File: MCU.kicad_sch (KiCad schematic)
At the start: 30 parts, among them J1 HSEC8-150-01-X-RA-X, J17 Conn_02x30_Counter_Clockwise, J2 Barrel_Jack_MountingPin, J22 Conn_01x02, J23 Conn_01x02, J4 Conn_02x30_Counter_Clockwise, J6 Conn_01x02, U3 LMR36510ADDA

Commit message: Validated for prod
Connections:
- net PE10_EXTI10: no longer names the net of J4.39 (Pin_39)
- no-connect marks 17 -> 24
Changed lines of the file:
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@@
 	)
 	(no_connect
+		(at 190.5 262.89)
+	)
+	(no_connect
+		(at 190.5 265.43)
+	)
+	(no_connect
 		(at 167.64 78.74)
 	)
@@
 	)
 	(no_connect
+		(at 95.25 245.11)
+	)
+	(no_connect
 		(at 116.84 63.5)
 	)
 	(no_connect
+		(at 95.25 247.65)
+	)
+	(no_connect
 		(at 116.84 81.28)
 	)
@@
 	)
 	(no_connect
+		(at 95.25 252.73)
+	)
+	(no_connect
 		(at 91.44 45.72)
 	)
@@
 	)
 	(no_connect
+		(at 95.25 255.27)
+	)
+	(no_connect
 		(at 193.04 68.58)
 	)
@@
 		(at 91.44 91.44)
 	)
+	(no_connect
+		(at 190.5 260.35)
+	)
 	(wire
 		(pts
@@
 	(wire
 		(pts
-			(xy 118.11 99.06) (xy 116.84 99.06)
+			(xy 116.84 99.06) (xy 119.38 99.06)
 		)
 		(stroke
@@
 	(wire
 		(pts
-			(xy 116.84 96.52) (xy 118.11 96.52)
+			(xy 116.84 96.52) (xy 119.38 96.52)
 		)
 		(stroke
@@
 	(wire
 		(pts
-			(xy 116.84 55.88) (xy 118.11 55.88)
+			(xy 116.84 55.88) (xy 119.38 55.88)
 		)
 		(stroke
@@
 	(wire
 		(pts
-			(xy 116.84 68.58) (xy 118.11 68.58)
+			(xy 116.84 68.58) (xy 119.38 68.58)
 		)
 		(stroke
@@
 	(wire
 		(pts
-			(xy 116.84 91.44) (xy 118.11 91.44)
+			(xy 116.84 91.44) (xy 119.38 91.44)
 		)
 		(stroke
@@
 	(wire
 		(pts
-			(xy 95.25 245.11) (xy 99.06 245.11)
-		)
-		(stroke
-			(width 0)
-			(type default)
-		)
-	)
-	(wire
-		(pts
 			(xy 187.96 229.87) (xy 190.5 229.87)
 		)
@@
 	(wire
 		(pts
-			(xy 116.84 53.34) (xy 118.11 53.34)
+			(xy 116.84 53.34) (xy 119.38 53.34)
 		)
 		(stroke
@@
 	(wire
 		(pts
-			(xy 116.84 88.9) (xy 118.11 88.9)
+			(xy 116.84 88.9) (xy 119.38 88.9)
 		)
 		(stroke
@@
 	(wire
 		(pts
-			(xy 116.84 71.12) (xy 118.11 71.12)
+			(xy 116.84 71.12) (xy 119.38 71.12)
 		)
 		(stroke
@@
 	(wire
 		(pts
-			(xy 116.84 78.74) (xy 118.11 78.74)
+			(xy 116.84 78.74) (xy 119.38 78.74)
 		)
 		(stroke
@@
 	(global_label "ISOSW_HOLD_CMD"
 		(shape input)
-		(at 118.11 99.06 0)
+		(at 119.38 99.06 0)
 		(fields_autoplaced yes)
 		(effects
@@
 		)
 		(property "Intersheetrefs" "${INTERSHEET_REFS}"
-			(at 141.1732 99.06 0)
+			(at 142.4432 99.06 0)
 			(hide yes)
 			(show_name no)
@@
 	(global_label "ISOSW_OF_ST"
 		(shape input)
-		(at 118.11 88.9 0)
+		(at 119.38 88.9 0)
 		(fields_autoplaced yes)
 		(effects
@@
 		)
 		(property "Intersheetrefs" "${INTERSHEET_REFS}"
-			(at 136.8189 88.9 0)
+			(at 138.0889 88.9 0)
 			(hide yes)
 			(show_name no)
@@
 	(global_label "A0V"
 		(shape input)
-		(at 118.11 71.12 0)
+		(at 119.38 71.12 0)
 		(fields_autoplaced yes)
 		(effects
@@
 		)
 		(property "Intersheetrefs" "${INTERSHEET_REFS}"
-			(at 124.4819 71.12 0)
+			(at 125.7519 71.12 0)
 			(hide yes)
 			(show_name no)
@@
 	(global_label "PADLOCK_OF"
 		(shape input)
-		(at 118.11 96.52 0)
+		(at 119.38 96.52 0)
 		(fields_autoplaced yes)
 		(effects
@@
 		)
 		(property "Intersheetrefs" "${INTERSHEET_REFS}"
-			(at 136.3957 96.52 0)
+			(at 137.6657 96.52 0)
 			(hide yes)
 			(show_name no)
@@
 		)
 	)
-	(global_label "PE10_EXTI10"
-		(shape input)
-		(at 99.06 245.11 0)
-		(fields_autoplaced yes)
-		(effects
-			(font
-				(size 1.27 1.27)
-			)
-			(justify left)
-		)
-		(property "Intersheetrefs" "${INTERSHEET_REFS}"
-			(at 114.2007 245.11 0)
-			(hide yes)
-			(show_name no)
-			(do_not_autoplace no)
-			(effects
-				(font
-					(size 1.27 1.27)
-				)
-				(justify left)
-			)
-		)
-	)
 	(global_label "V_ACT"
 		(shape input)
@@
 	(global_label "SDMOS"
 		(shape input)
-		(at 118.11 68.58 0)
+		(at 119.38 68.58 0)
 		(fields_autoplaced yes)
 		(effects
@@
 		)
 		(property "Intersheetrefs" "${INTERSHEET_REFS}"
-			(at 130.9527 68.58 0)
+			(at 132.2227 68.58 0)
 			(hide yes)
 			(show_name no)
@@
 	(global_label "VPS_P24V_PG"
 		(shape input)
-		(at 118.11 78.74 0)
+		(at 119.38 78.74 0)
 		(fields_autoplaced yes)
 		(effects
@@
 		)
 		(property "Intersheetrefs" "${INTERSHEET_REFS}"
-			(at 137.3027 78.74 0)
+			(at 138.5727 78.74 0)
 			(hide yes)
 			(show_name no)
@@
 	(global_label "OPCL_DS"
 		(shape input)
-		(at 118.11 53.34 0)
+		(at 119.38 53.34 0)
 		(fields_autoplaced yes)
 		(effects
@@
 		)
 		(property "Intersheetrefs" "${INTERSHEET_REFS}"
-			(at 132.8275 53.34 0)
+			(at 134.0975 53.34 0)
 			(hide yes)
 			(show_name no)
@@
 	(global_label "A0V"
 		(shape input)
-		(at 118.11 55.88 0)
+		(at 119.38 55.88 0)
 		(fields_autoplaced yes)
 		(effects
@@
 		)
 		(property "Intersheetrefs" "${INTERSHEET_REFS}"
-			(at 124.4819 55.88 0)
+			(at 125.7519 55.88 0)
 			(hide yes)
 			(show_name no)
@@
 	(global_label "ISOSW_INRUSH_CMD"
 		(shape input)
-		(at 118.11 91.44 0)
+		(at 119.38 91.44 0)
 		(fields_autoplaced yes)
 		(effects
@@
 		)
 		(property "Intersheetrefs" "${INTERSHEET_REFS}"
-			(at 143.2899 91.44 0)
+			(at 144.5599 91.44 0)
 			(hide yes)
 			(show_name no)

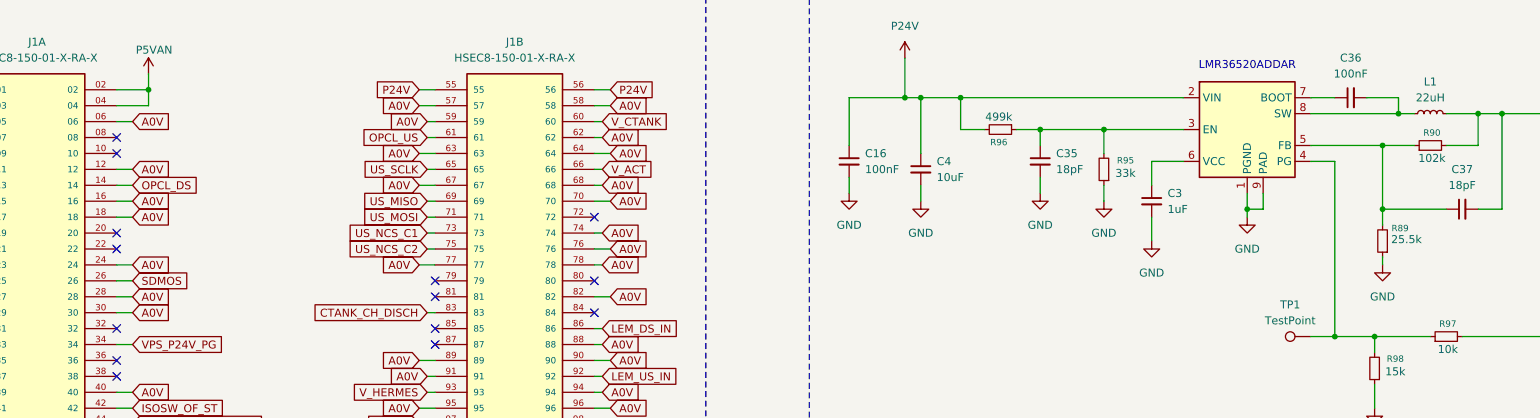
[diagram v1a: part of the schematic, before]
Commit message: breakout typo
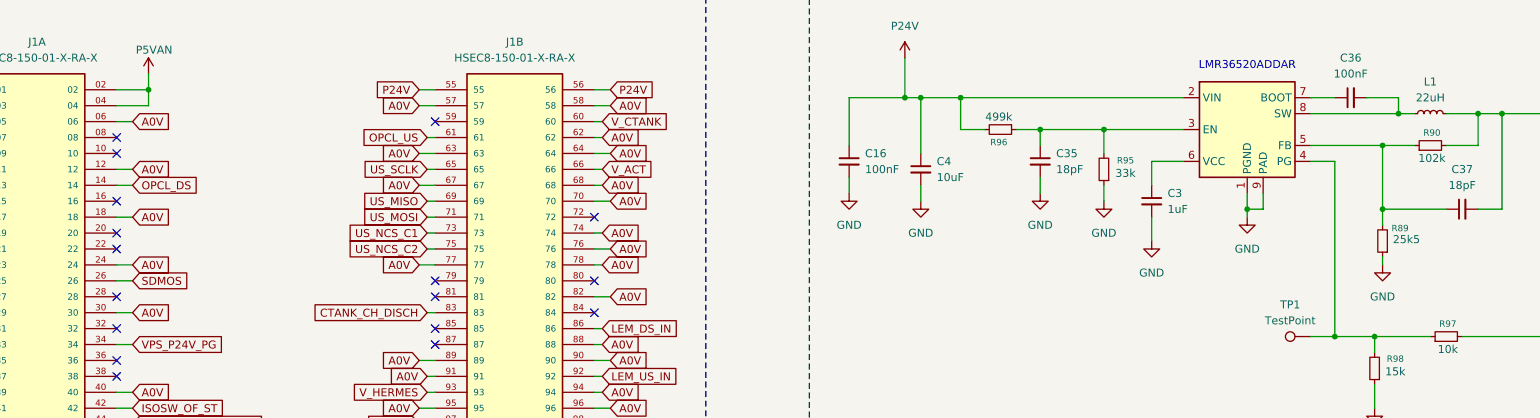
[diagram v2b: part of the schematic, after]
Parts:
- R89: value 25.5k -> 25k5
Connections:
- net GND: no longer J1.16, J1.28, J1.59
- no-connect marks 24 -> 27
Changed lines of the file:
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@@
 	)
 	(no_connect
+		(at 167.64 43.18)
+	)
+	(no_connect
 		(at 193.04 58.42)
 	)
@@
 	)
 	(no_connect
+		(at 116.84 55.88)
+	)
+	(no_connect
 		(at 116.84 60.96)
 	)
@@
 	)
 	(no_connect
+		(at 116.84 71.12)
+	)
+	(no_connect
 		(at 190.5 260.35)
 	)
@@
 	(wire
 		(pts
-			(xy 116.84 55.88) (xy 119.38 55.88)
-		)
-		(stroke
-			(width 0)
-			(type default)
-		)
-	)
-	(wire
-		(pts
 			(xy 167.64 91.44) (xy 165.1 91.44)
 		)
@@
 	(wire
 		(pts
-			(xy 116.84 71.12) (xy 119.38 71.12)
-		)
-		(stroke
-			(width 0)
-			(type default)
-		)
-	)
-	(wire
-		(pts
 			(xy 80.01 222.25) (xy 82.55 222.25)
 		)
@@
 	(wire
 		(pts
-			(xy 167.64 43.18) (xy 166.37 43.18)
-		)
-		(stroke
-			(width 0)
-			(type default)
-		)
-	)
-	(wire
-		(pts
 			(xy 255.27 44.45) (xy 251.46 44.45)
 		)
@@
 		)
 	)
-	(global_label "A0V"
-		(shape input)
-		(at 166.37 43.18 180)
-		(fields_autoplaced yes)
-		(effects
-			(font
-				(size 1.27 1.27)
-			)
-			(justify right)
-		)
-		(property "Intersheetrefs" "${INTERSHEET_REFS}"
-			(at 159.9981 43.18 0)
-			(hide yes)
-			(show_name no)
-			(do_not_autoplace no)
-			(effects
-				(font
-					(size 1.27 1.27)
-				)
-				(justify right)
-			)
-		)
-	)
 	(global_label "ISOSW_HOLD_CMD"
 		(shape input)
@@
 		)
 	)
-	(global_label "A0V"
-		(shape input)
-		(at 119.38 71.12 0)
-		(fields_autoplaced yes)
-		(effects
-			(font
-				(size 1.27 1.27)
-			)
-			(justify left)
-		)
-		(property "Intersheetrefs" "${INTERSHEET_REFS}"
-			(at 125.7519 71.12 0)
-			(hide yes)
-			(show_name no)
-			(do_not_autoplace no)
-			(effects
-				(font
-					(size 1.27 1.27)
-				)
-				(justify left)
-			)
-		)
-	)
 	(global_label "US_MISO"
 		(shape input)
@@
 	(global_label "A0V"
 		(shape input)
-		(at 119.38 55.88 0)
-		(fields_autoplaced yes)
-		(effects
-			(font
-				(size 1.27 1.27)
-			)
-			(justify left)
-		)
-		(property "Intersheetrefs" "${INTERSHEET_REFS}"
-			(at 125.7519 55.88 0)
-			(hide yes)
-			(show_name no)
-			(do_not_autoplace no)
-			(effects
-				(font
-					(size 1.27 1.27)
-				)
-				(justify left)
-			)
-		)
-	)
-	(global_label "A0V"
-		(shape input)
 		(at 194.31 86.36 0)
 		(fields_autoplaced yes)
@@
 			)
 		)
-		(property "Value" "25.5k"
+		(property "Value" "25k5"
 			(at 322.58 61.976 0)
 			(show_name no)

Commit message: Go vertical + BOM
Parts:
- removed J1: HSEC8-150-01-X-RA-X, kicad_jlcpcb_hil_mcu_ep2:SAMTEC_HSEC8-150-01-X-RA-X, symbol HSEC8-150-01-X-RA-X:HSEC8-150-01-X-RA-X
- added J1: HSEC8-150-01-X-DV-A, Connector_Samtec_HSEC8:Samtec_HSEC8-150-01-X-DV-A_2x50_P0.8mm_Pol27_Socket_AlignmentPins, symbol HSEC8-150-01-X-DV-A:HSEC8-150-01-X-DV-A
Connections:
- net CTANK_CH_DISCH: now also J1.83
- net DS_MISO: now also J1.21
- net DS_MOSI: now also J1.19
- net DS_NCS_C1: now also J1.15
- net DS_NCS_C2: now also J1.13
- net DS_SCLK: now also J1.25
- net EN_PS_ACT: now also J1.47
- net GND: now also J1.100, J1.11, J1.12, J1.17, J1.18, J1.23, J1.24, J1.27, J1.29, J1.30, J1.33, J1.35, J1.39, J1.40, J1.45, J1.46, J1.5, J1.51, J1.52, J1.57, J1.58, J1.6, J1.62, J1.63, J1.64, J1.67, J1.68, J1.70, J1.74, J1.76, J1.77, J1.78, J1.82, J1.88, J1.89, J1.9, J1.90, J1.91, J1.94, J1.95, J1.96, J1.98
- net ISOSW_HOLD_CMD: now also J1.50
- net ISOSW_INRUSH_CMD: now also J1.44
- net ISOSW_OF_ST: now also J1.42
- net LEM_DS_IN: now also J1.86
- net LEM_US_IN: now also J1.92
- net OPCL_DS: now also J1.14
- net OPCL_US: now also J1.61
- net P24V: now also J1.53, J1.54, J1.55, J1.56
- net P5VAN: now also J1.1, J1.2, J1.3, J1.4, J1.97, J1.99
- net PADLOCK_OF: now also J1.48
- net SDMOS: now also J1.26
- net SSR_CTL: now also J1.41
- net US_MISO: now also J1.69
- net US_MOSI: now also J1.71
- net US_NCS_C1: now also J1.73
- net US_NCS_C2: now also J1.75
- net US_SCLK: now also J1.65
- net VPS_P24V_PG: now also J1.34
- net V_ACT: now also J1.66
- net V_CTANK: now also J1.60
- net V_DS: now also J1.37
- net V_HERMES: now also J1.93
- net V_US: now also J1.31
- no-connect marks 27 -> 28

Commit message: Production JLCPCB via France
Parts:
- C4: footprint Capacitor_SMD:C_0603_1608Metric -> Capacitor_SMD:C_0805_2012Metric
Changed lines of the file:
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@@
 			)
 		)
-		(property "Footprint" "Capacitor_SMD:C_0603_1608Metric"
+		(property "Footprint" "Capacitor_SMD:C_0805_2012Metric"
 			(at 245.11 50.8 0)
 			(hide yes)
